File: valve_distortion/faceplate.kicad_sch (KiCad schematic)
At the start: 7 parts

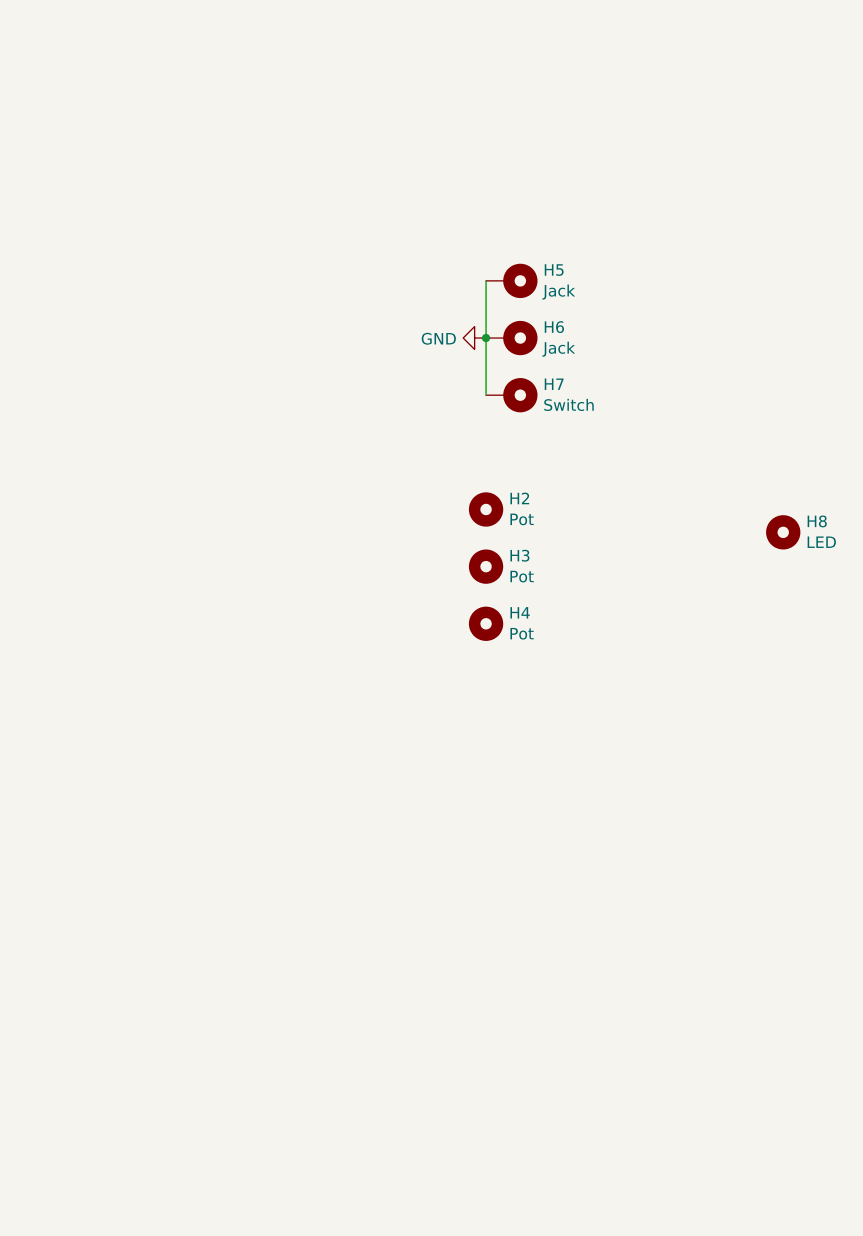
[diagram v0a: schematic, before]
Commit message: Add complete files for valve distortion euro module
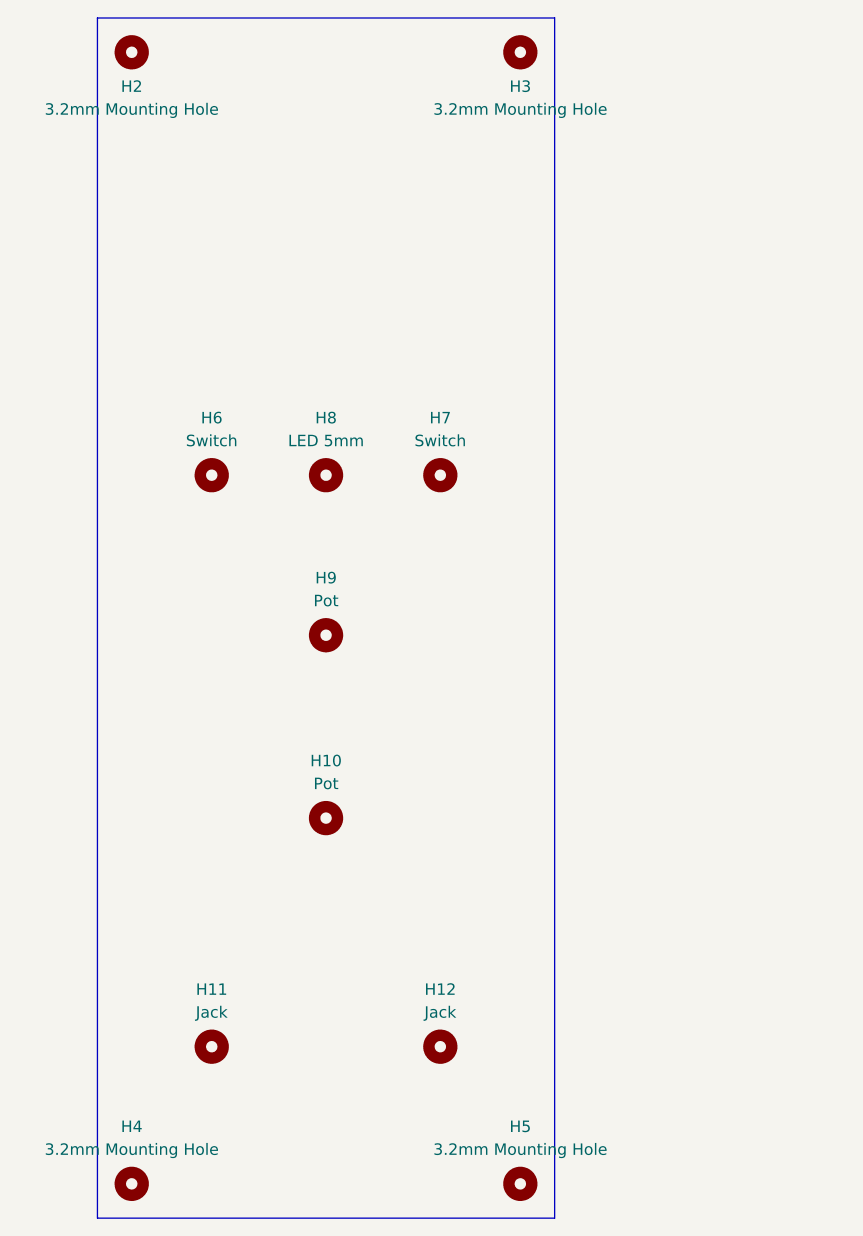
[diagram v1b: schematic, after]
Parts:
- removed H5, H6: Jack, kosmo-lib:Hole_Jack, symbol Mechanical:MountingHole_Pad
- removed H7: Switch, MountingHole:MountingHole_6.4mm_M6_ISO14580_Pad, symbol Mechanical:MountingHole_Pad
- added H10, H9: Pot, kosmo-lib:Hole_Pot, symbol Mechanical:MountingHole
- added H11, H12: Jack, kosmo-lib:Hole_Jack_3.5mm, symbol Mechanical:MountingHole
- added H2, H5: 3.2mm Mounting Hole, MountingHole:MountingHole_3.2mm_M3, symbol Mechanical:MountingHole
- added H7: Switch, kosmo-lib:Hole_Toggle_Switch, symbol Mechanical:MountingHole
- H3, H4: value Pot -> 3.2mm Mounting Hole; footprint kosmo-lib:Hole_Pot -> MountingHole:MountingHole_3.2mm_M3
- H6: renamed from H2; value Pot -> Switch; footprint kosmo-lib:Hole_Pot -> kosmo-lib:Hole_Toggle_Switch
- H8: value LED -> LED 5mm; footprint MountingHole:MountingHole_5mm -> kosmo-lib:Hole_LED_5mm
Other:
- company: (none) -> Max Proskauer
- title: (none) -> Valve Distortion Euro Module
- moved on the sheet: H6
